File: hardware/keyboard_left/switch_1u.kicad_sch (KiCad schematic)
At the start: 4 parts

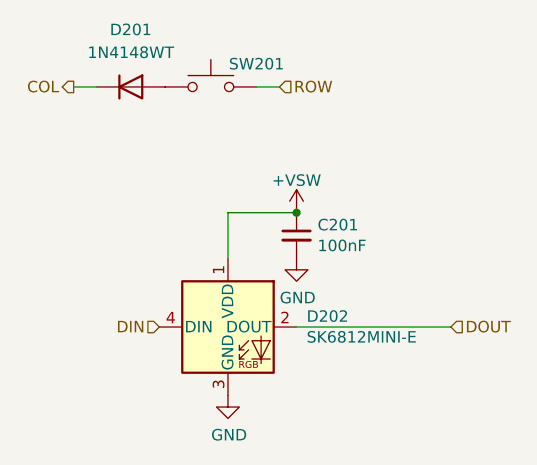
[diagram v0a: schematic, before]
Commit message: Update after producion of rev 2
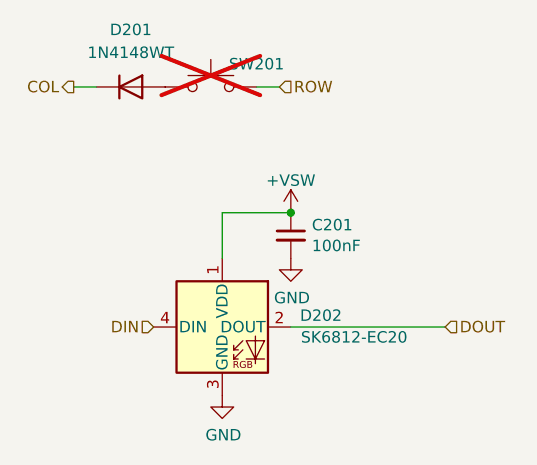
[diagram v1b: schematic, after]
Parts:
- C201: footprint Capacitor_SMD:C_0603_1608Metric_Pad1.08x0.95mm_HandSolder -> Capacitor_SMD:C_0402_1005Metric; LCSC (none) -> C1525
- D201: LCSC (none) -> C27748
- D202: value SK6812MINI-E -> SK6812-EC20; footprint prettylib:SK6812MINI-E-reversible -> prettylib:sk6812-ec20; LCSC (none) -> C2909058
- SW201: now not fitted
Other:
- moved on the sheet: C201, D202
